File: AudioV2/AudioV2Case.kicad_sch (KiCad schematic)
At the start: 0 parts

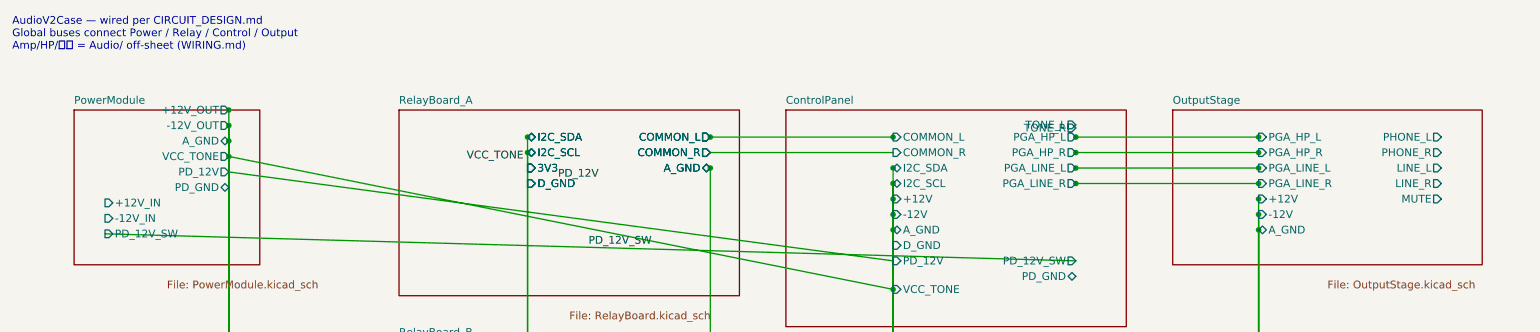
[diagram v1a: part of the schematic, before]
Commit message: feat(AudioV2): 手回し音量構成へ回路図を改訂
- PT2314 を Princeton DS どおり 28pin DIP シンボルに再作成
- PGA2310 / DEST ラッチング / ENC×6 を削除
- OutputStage: SW_DP3T + A50k Dual×2（AMP_SEL→PHONE/LINE）
- ControlPanel: ENC×3 + DEST ラダー(10k/10k/1k) + LED
- CIRCUIT_DESIGN.md を DS 照合・手回し方針に更新
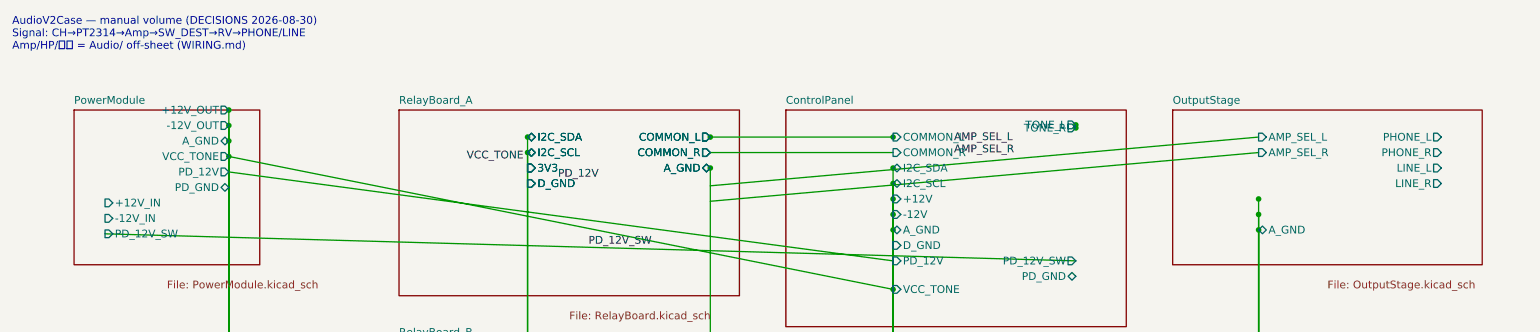
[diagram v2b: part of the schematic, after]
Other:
- sheet ControlPanel ports: added none; removed PGA_HP_L, PGA_HP_R, PGA_LINE_L, PGA_LINE_R
- sheet OutputStage ports: added AMP_SEL_L, AMP_SEL_R; removed +12V, -12V, MUTE, PGA_HP_L, PGA_HP_R, PGA_LINE_L, PGA_LINE_R
- note added: "AudioV2Case — manual volume (DECISIONS 2026-08-30) Signal: CH→PT2314→Amp→SW_DEST→RV→PHONE/LINE Amp/HP/計測 = Audio/ off-sheet (WIRING.md)"
- note removed: "AudioV2Case — wired per CIRCUIT_DESIGN.md Global buses connect Power / Relay / Control / Output Amp/HP/計測 = Audio/ off-sheet (WIRING.md)"
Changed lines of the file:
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@@
 	(generator_version "10.0")
 	(paper "A4")
-	(text "AudioV2Case — wired per CIRCUIT_DESIGN.md\nGlobal buses connect Power / Relay / Control / Output\nAmp/HP/計測 = Audio/ off-sheet (WIRING.md)"
+	(text "AudioV2Case — manual volume (DECISIONS 2026-08-30)\nSignal: CH→PT2314→Amp→SW_DEST→RV→PHONE/LINE\nAmp/HP/計測 = Audio/ off-sheet (WIRING.md)"
 		(at 25.4 20.32 0)
 		(effects
@@
 			)
 		)
-		(pin "PGA_HP_L" output
-			(at 200.0 40.0 0)
-			(effects
-				(font
-					(size 1.27 1.27)
-				)
-				(justify right)
-			)
-		)
-		(pin "PGA_HP_R" output
-			(at 200.0 42.54 0)
-			(effects
-				(font
-					(size 1.27 1.27)
-				)
-				(justify right)
-			)
-		)
-		(pin "PGA_LINE_L" output
-			(at 200.0 45.08 0)
-			(effects
-				(font
-					(size 1.27 1.27)
-				)
-				(justify right)
-			)
-		)
-		(pin "PGA_LINE_R" output
-			(at 200.0 47.62 0)
-			(effects
-				(font
-					(size 1.27 1.27)
-				)
-				(justify right)
-			)
-		)
 		(pin "VCC_TONE" input
 			(at 170.0 65.0 180)
@@
 			)
 		)
-		(pin "PGA_HP_L" input
+		(pin "AMP_SEL_L" input
 			(at 230.0 40.0 180)
 			(effects
@@
 			)
 		)
-		(pin "PGA_HP_R" input
+		(pin "AMP_SEL_R" input
 			(at 230.0 42.54 180)
-			(effects
-				(font
-					(size 1.27 1.27)
-				)
-				(justify left)
-			)
-		)
-		(pin "PGA_LINE_L" input
-			(at 230.0 45.08 180)
-			(effects
-				(font
-					(size 1.27 1.27)
-				)
-				(justify left)
-			)
-		)
-		(pin "PGA_LINE_R" input
-			(at 230.0 47.62 180)
-			(effects
-				(font
-					(size 1.27 1.27)
-				)
-				(justify left)
-			)
-		)
-		(pin "+12V" input
-			(at 230.0 50.16 180)
-			(effects
-				(font
-					(size 1.27 1.27)
-				)
-				(justify left)
-			)
-		)
-		(pin "-12V" input
-			(at 230.0 52.7 180)
 			(effects
 				(font
@@
 		(pin "LINE_R" output
 			(at 260.0 47.62 0)
-			(effects
-				(font
-					(size 1.27 1.27)
-				)
-				(justify right)
-			)
-		)
-		(pin "MUTE" output
-			(at 260.0 50.16 0)
 			(effects
 				(font
@@
 		(color 0 0 0 0)
 	)
-	(wire
-		(pts
-			(xy 200.0 40.0) (xy 230.0 40.0)
-		)
-		(stroke
-			(width 0)
-			(type default)
-		)
-	)
-	(junction
-		(at 200.0 40.0)
-		(diameter 0)
-		(color 0 0 0 0)
-	)
-	(junction
-		(at 230.0 40.0)
-		(diameter 0)
-		(color 0 0 0 0)
-	)
-	(wire
-		(pts
-			(xy 200.0 42.54) (xy 230.0 42.54)
-		)
-		(stroke
-			(width 0)
-			(type default)
-		)
-	)
-	(junction
-		(at 200.0 42.54)
-		(diameter 0)
-		(color 0 0 0 0)
-	)
-	(junction
-		(at 230.0 42.54)
-		(diameter 0)
-		(color 0 0 0 0)
-	)
-	(wire
-		(pts
-			(xy 200.0 45.08) (xy 230.0 45.08)
-		)
-		(stroke
-			(width 0)
-			(type default)
-		)
-	)
-	(junction
-		(at 200.0 45.08)
-		(diameter 0)
-		(color 0 0 0 0)
-	)
-	(junction
-		(at 230.0 45.08)
-		(diameter 0)
-		(color 0 0 0 0)
-	)
-	(wire
-		(pts
-			(xy 200.0 47.62) (xy 230.0 47.62)
-		)
-		(stroke
-			(width 0)
-			(type default)
-		)
-	)
-	(junction
-		(at 200.0 47.62)
-		(diameter 0)
-		(color 0 0 0 0)
-	)
-	(junction
-		(at 230.0 47.62)
-		(diameter 0)
-		(color 0 0 0 0)
-	)
-	(wire
+	(junction
+		(at 200.0 38.0)
+		(diameter 0)
+		(color 0 0 0 0)
+	)
+	(junction
+		(at 200.0 38.5)
+		(diameter 0)
+		(color 0 0 0 0)
+	)
+	(wire
+		(pts
+			(xy 140.0 48.0) (xy 230.0 40.0)
+		)
+		(stroke
+			(width 0)
+			(type default)
+		)
+	)
+	(wire
+		(pts
+			(xy 140.0 50.54) (xy 230.0 42.54)
+		)
+		(stroke
+			(width 0)
+			(type default)
+		)
+	)
+	(label "AMP_SEL_L"
+		(at 180 41 0)
+		(effects
+			(font
+				(size 1.27 1.27)
+			)
+			(justify left bottom)
+		)
+	)
+	(label "AMP_SEL_R"
+		(at 180 43 0)
+		(effects
+			(font
+				(size 1.27 1.27)
+			)
+			(justify left bottom)
+		)
+	)
+	(wire

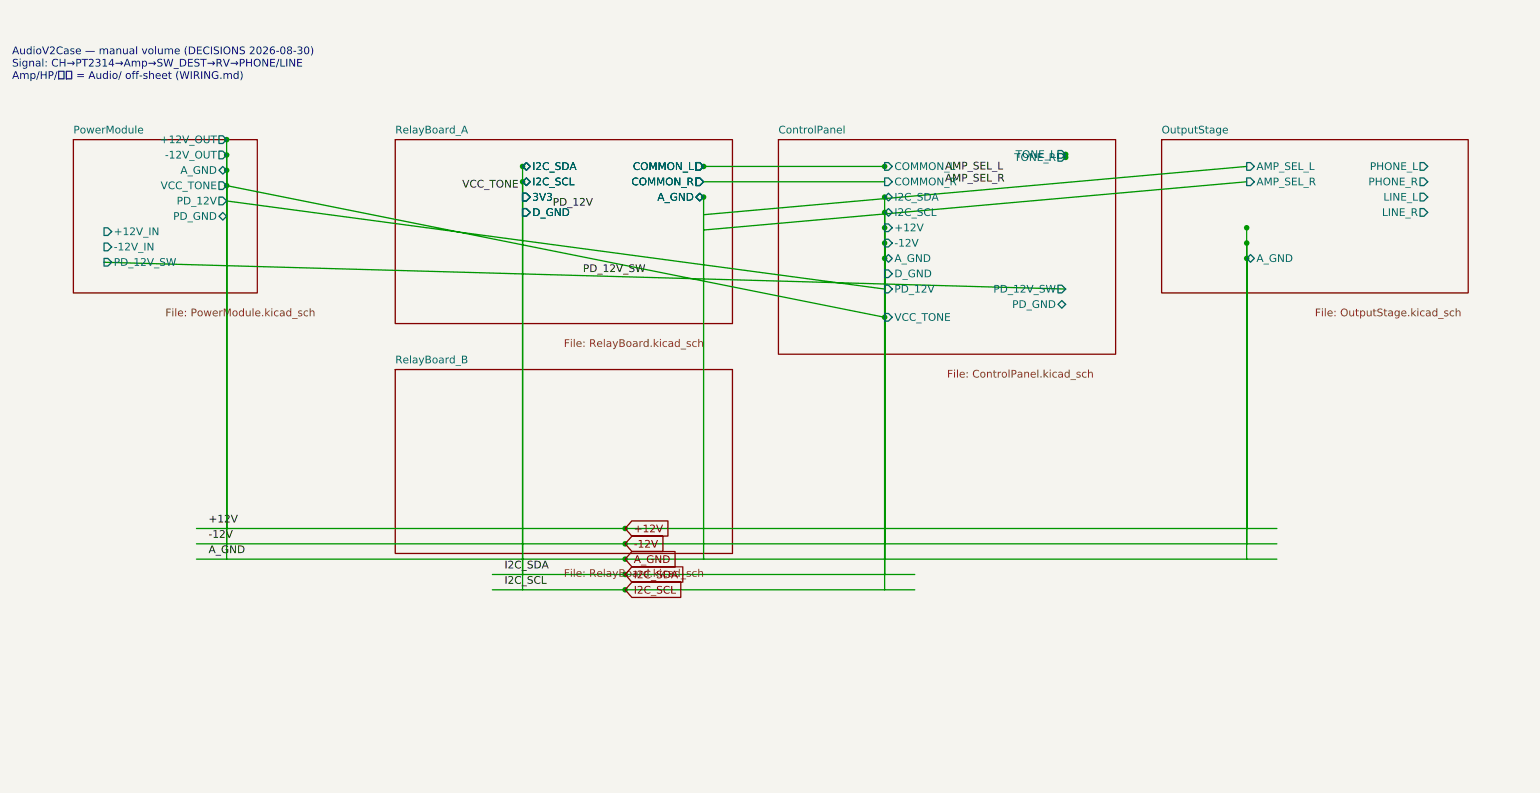
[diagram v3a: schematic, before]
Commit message: AudioV2: ラベル結線で Power/Control/Output をネット接続
pin_connect を tip=(at) 基準に修正し、同名ローカルラベルをピン tip に
載せて結線。グリッドスナップ一致・パッシブ間隔・親シートピン橋渡しを
整え、一次 PD_GND と二次 A_GND の分離を維持。
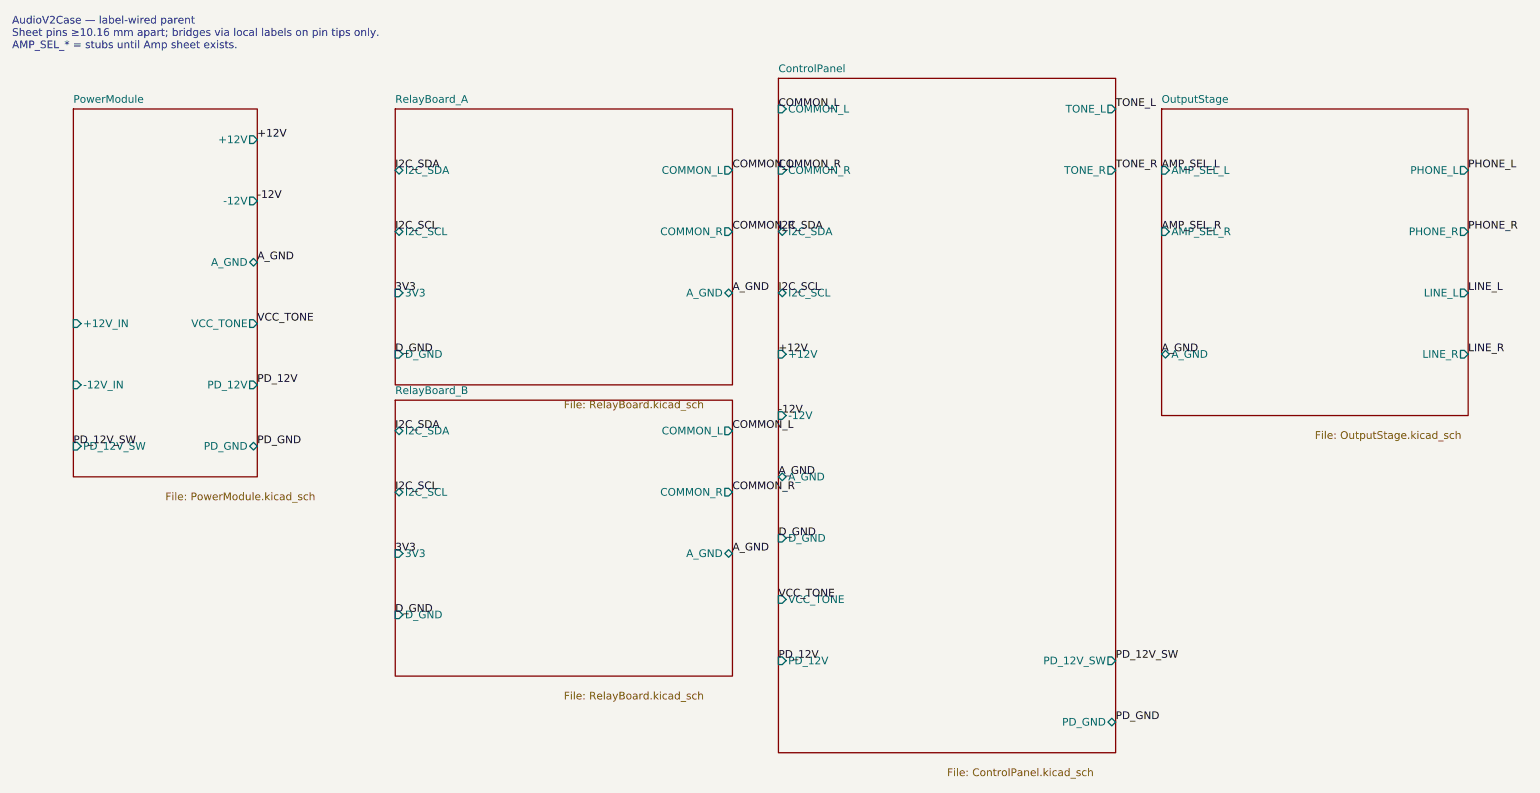
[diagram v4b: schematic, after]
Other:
- sheet PowerModule ports: added +12V, -12V; removed +12V_OUT, -12V_OUT
- note added: "AudioV2Case — label-wired parent Sheet pins ≥10.16 mm apart; bridges via local labels on pin tips only. AMP_SEL_* = stubs until Amp sheet exists."
- note removed: "AudioV2Case — manual volume (DECISIONS 2026-08-30) Signal: CH→PT2314→Amp→SW_DEST→RV→PHONE/LINE Amp/HP/計測 = Audio/ off-sheet (WIRING.md)"
